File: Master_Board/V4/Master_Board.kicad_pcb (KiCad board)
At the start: 2 copper layers, 138.4 x 96.5 mm, 216 parts, among them J1001 61400416121, J101 649002227222, J102 649002227222, J103 649002227222, J104 649006227222, J201 Header_Male_Pin_2.54mm_1X3_,_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, J202 Header_Male_Pin_2.54mm_1X6_,_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, J301 Header_Male_Pin_2.54mm_1X2_,_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, J401 649006227222, J601 649004227222, J701 649004227222, J702 649004227222, J703 649004227222, J704 649002227222, J801 649002227222, J802 649002227222, J803 649002227222, J804 649002227222, Q1101 BSS806NH6327XTSA1, Q1102 BSS806NH6327XTSA1, Q1103 BSS806NH6327XTSA1, Q601 BC849BLT1G, Q701 BC849BLT1G, Q702 BC849BLT1G, Q703 BC849BLT1G, Q704 BC849BLT1G, Q801 BC849BLT1G, Q802 BC849BLT1G, Q803 BSS806NH6327XTSA1, SW201 PTS645SM43SMTR92, SW202 PTS645SM43SMTR92, U201 STM32F446RE, U301 OKI-78SR-5_1.5-W36H-C, U302 AZ1117IH-3.3TRG1, U401 SN65HVD232DR, U501 SN65HVD232DR, U601 TLP3543A(TP1,F, U602 TLP3543A(TP1,F, U603 TLP3543A(TP1,F, U604 TLP3543A(TP1,F, U605 TLP3543A(TP1,F, U701 CPC1117NTR, U901 ACPL-C87A-500E, U902 NCS1S2405SC, U903 ACPL-C87A-500E, U904 LMV321RILT, U905 LMV321RILT, U906 CPC1117NTR

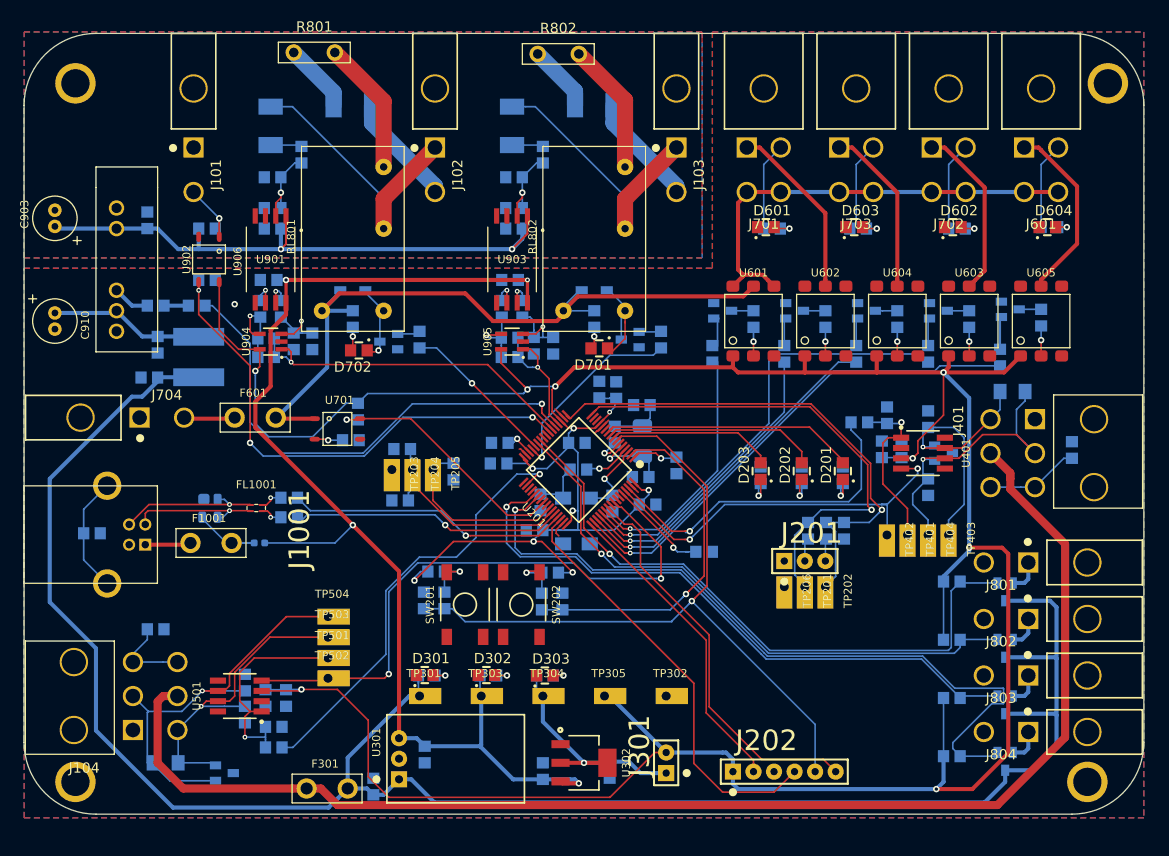
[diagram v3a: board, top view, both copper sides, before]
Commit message: Reanotate all schematic and finish routing
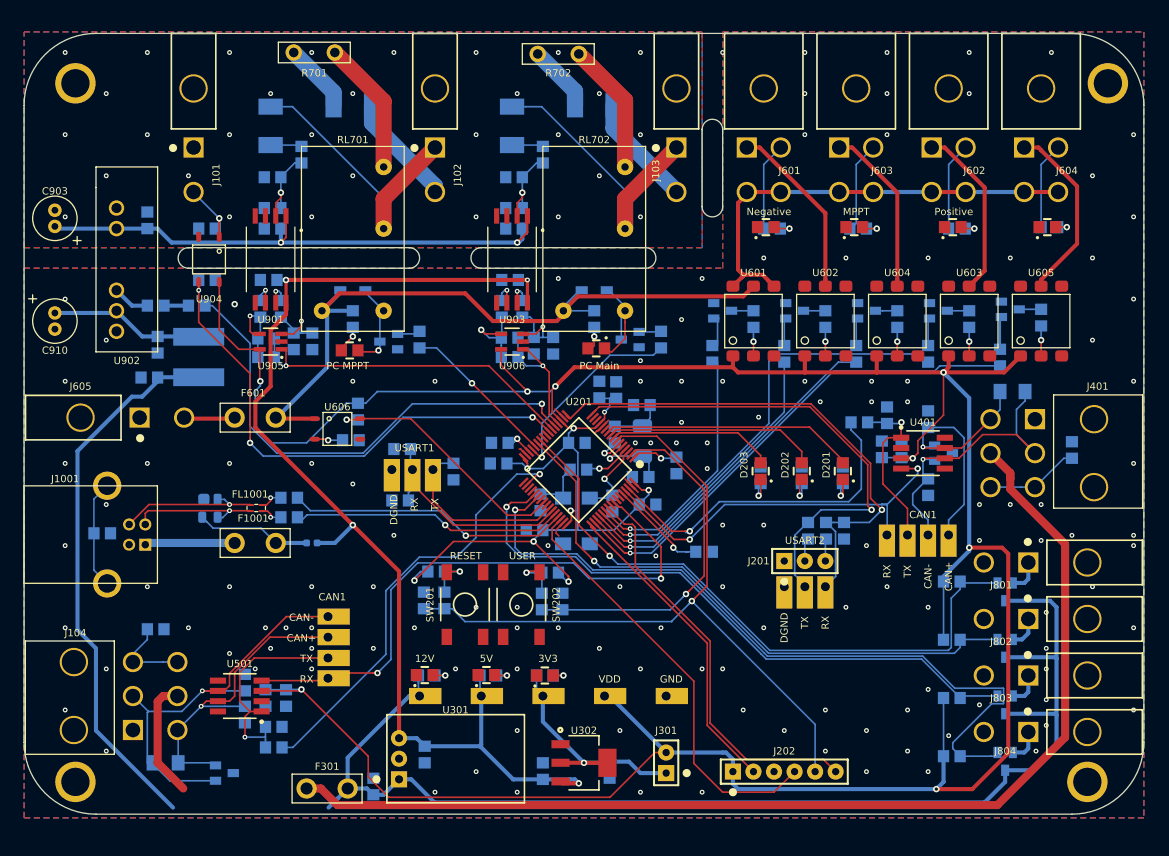
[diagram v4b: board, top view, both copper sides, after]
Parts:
- removed the Q601 at (205.2, 71.4)
- added Q605: BC849BLT1G, IC:SOT-23-3, B.Cu at (205.2, 71.4)
- moved FB1001 6.48 mm to (118.2, 100.3)
- moved F1001 5.46 mm to (111.9, 100.3)
- moved R1001 1.27 mm to (91.9, 99.1)
- moved D706 1.14 mm to (124.6, 76.5)
- moved D705 0.38 mm to (155.1, 76.3)
- renumbered D801 to D701, D802 to D702, D803 to D703, D804 to D704, D701 to D705, D702 to D706, J701 to J601, J702 to J602, J703 to J603, J601 to J604, J704 to J605, Q701 to Q601, Q702 to Q602, Q703 to Q603, Q704 to Q604, Q801 to Q701, Q802 to Q702, Q1101 to Q801, Q1102 to Q802, Q1103 to Q803, Q803 to Q804, R1005 to R1002, R1006 to R1003, R214 to R207, R207 to R208, R208 to R209, R209 to R210, R210 to R211, R211 to R212, R212 to R213, R213 to R214, R701 to R601, R702 to R602, R703 to R603, R704 to R604, R601 to R605, R705 to R606, R706 to R607, R707 to R608, R708 to R609, R602 to R610, R709 to R611, R710 to R612, R711 to R613, R603 to R614, R712 to R615, R713 to R616, R801 to R701, R802 to R702, R803 to R703, R804 to R704, R805 to R705, R806 to R706, R1002 to R801, R1003 to R802, R1004 to R803, R807 to R804, R914 to R905, R915 to R906, R905 to R907, R906 to R908, R907 to R909, R908 to R910, R909 to R911, R910 to R912, R911 to R913, R912 to R914, R913 to R915, RL801 to RL701, RL802 to RL702, U701 to U606, U906 to U904, U904 to U905, U905 to U906
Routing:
- net 12V: track 243.2 -> 221.1 mm
- net CAN_PWR: track 167.7 -> 152.5 mm
- net 5V: track 148.2 -> 141.7 mm
- net Net-(F1001-Pad1): track 5.68 -> 12.0 mm
- net Net-(D1001-Pad4): track 8.05 -> 14.2 mm
- net 5V_HP: track 75.1 -> 71.1 mm
- net VDD: track 450.0 -> 447.7 mm
- net Net-(C912-Pad2): track 8.83 -> 10.5 mm
- net /STM32F446/SWO: track 49.3 -> 50.4 mm
- net DGND: track 8.39 -> 9.46 mm, vias 1 -> 133
- net /USB/Shield_Connector: track 14.5 -> 13.4 mm
- net /PB1: track 72.2 -> 73.3 mm
- net /PB5: track 74.2 -> 73.3 mm
- net AGND: vias 0 -> 30
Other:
- outline, holes or cut-outs redrawn
- board text added: "12V"
- board text added: "3V3"
- board text added: "5V"
- board text added: "CAN+"
- board text added: "CAN-"
- board text added: "CAN1"
- board text added: "DGND"
- board text added: "GND"
- board text added: "MPPT"
- board text added: "Negative"
- board text added: "PC MPPT"
- board text added: "PC Main"
- board text added: "Positive"
- board text added: "RESET"
- board text added: "RX"
- board text added: "TX"
- board text added: "USART1"
- board text added: "USART2"
- board text added: "USER"
- board text added: "VDD"
